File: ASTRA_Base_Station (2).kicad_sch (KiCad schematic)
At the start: 24 parts, among them J2 24V, J3 24V, J4 24V, J5 5V, M1 Stepper_Motor_bipolar, U2 A4988_STEPPER_MOTOR_DRIVER_CA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, U4 D24V22F3, U5 D24V22F5, U6 D24V22F12

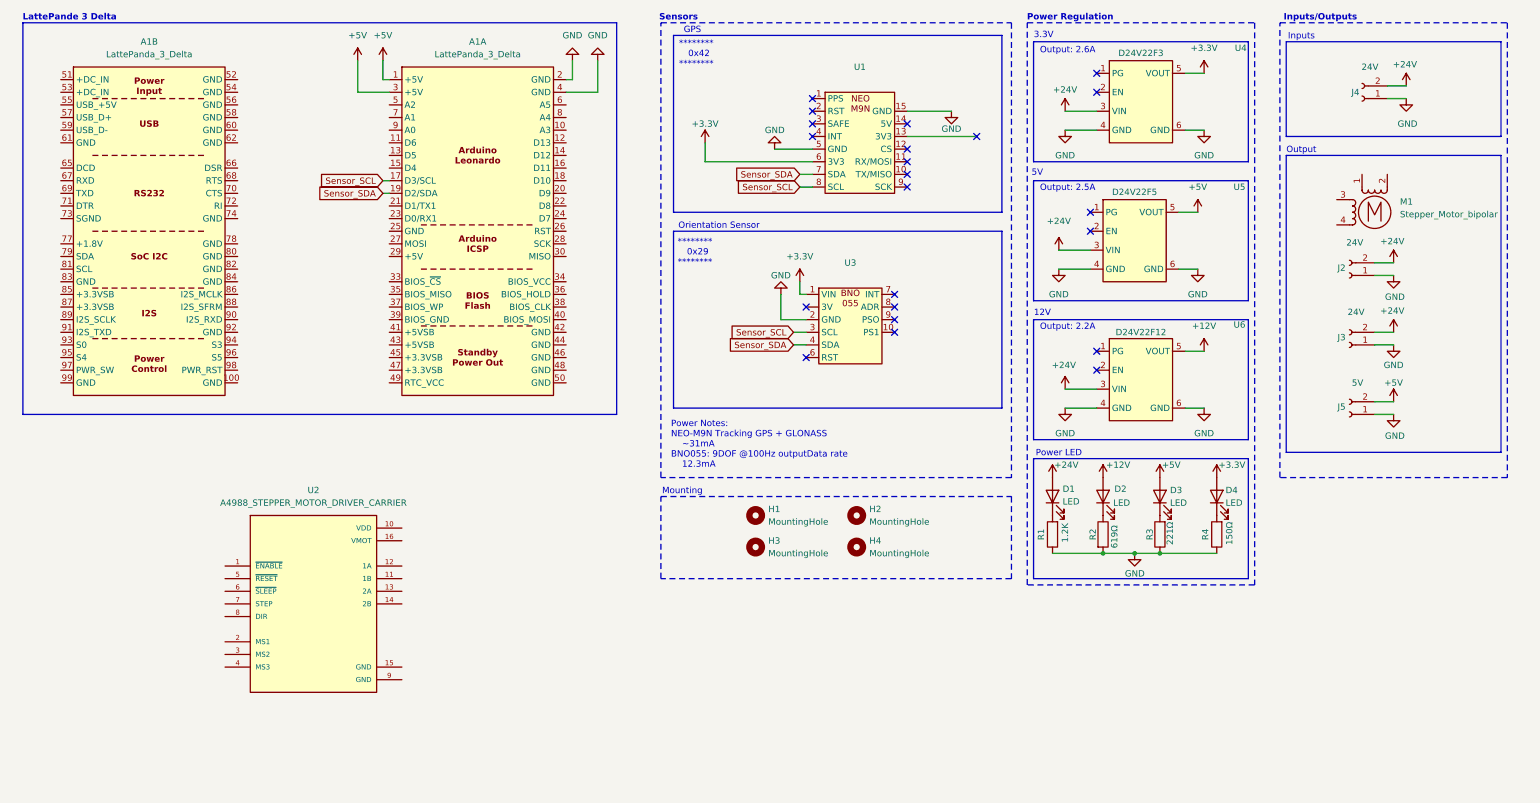
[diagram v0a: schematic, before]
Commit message: Added Motor Driver
Switched the motor driver from the A4988 to the more appropriate DRV8834, added schematic connections to the bipolar stepper motor, updated power regulation, organized schematic sections, and added the LattePanda Delta 3 and DRV8834 footprints to the tracking antenna library
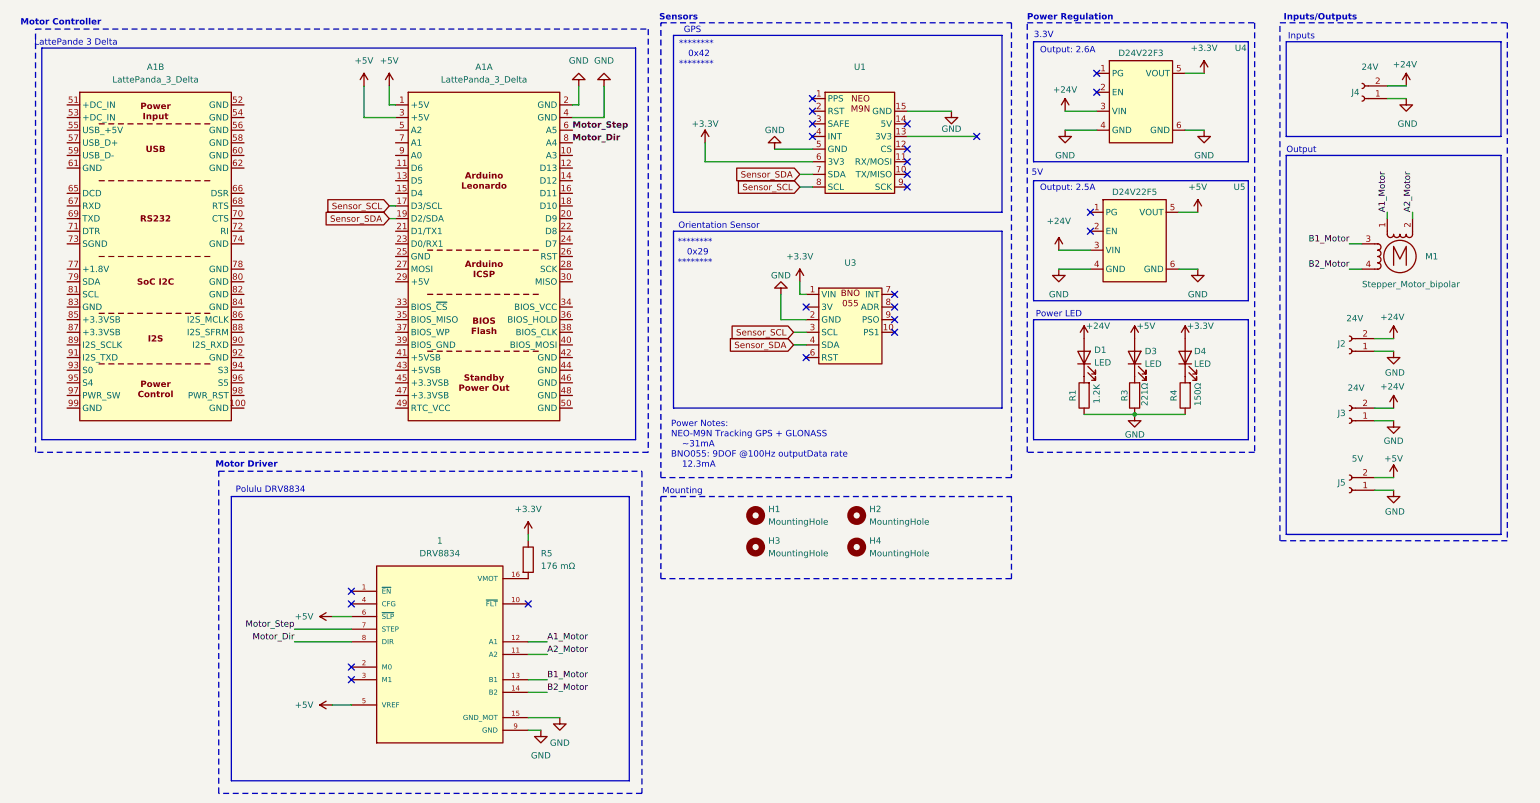
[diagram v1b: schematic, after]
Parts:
- removed D2: LED, Tracking Ant:LED 3mm, symbol Device:LED
- removed R2: 619Ω, Resistor_SMD:R_0603_1608Metric_Pad0.98x0.95mm_HandSolder, symbol Device:R
- removed U2: A4988_STEPPER_MOTOR_DRIVER_CARRIER, symbol Tracking_Antenna_25_Symbols:A4988_STEPPER_MOTOR_DRIVER_CARRIER
- removed U6: D24V22F12, Core_fp:D24V22Fx, symbol Tracking_Antenna_25_Symbols:D24V22Fx
- added 1: DRV8834, symbol Tracking_Antenna_25_Symbols:DRV8834
- added R5: 176 mΩ, symbol Device:R
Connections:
- net +3.3V: now also R5.1
- net +5V: now also 1.5 (VREF), 1.6 (~{SLP})
- net GND: now also 1.15 (GND_MOT), 1.9 (GND)
- net Motor_Step: now reaches A1.6 (A5)
- net Motor_Step: now also 1.7 (STEP)
- net Motor_Dir: now reaches A1.8 (A4)
- net Motor_Dir: now also 1.8 (DIR)
- net A1_Motor: now reaches M1.1
- net A1_Motor: now also 1.12 (A1)
- net A2_Motor: now reaches M1.2 (-)
- net A2_Motor: now also 1.11 (A2)
- net B1_Motor: now reaches M1.3
- net B1_Motor: now also 1.13 (B1)
- net B2_Motor: now reaches M1.4
- net B2_Motor: now also 1.14 (B2)
- new net: 1.16 (VMOT), R5.2
- no-connect marks 22 -> 25
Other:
- note added: "Motor Controller"
- note added: "Motor Driver"
- note added: "Polulu DRV8834"
- note removed: "12V"
- note removed: "Output: 2.2A"
- moved on the sheet: A1A, A1B, D1, D3, D4, J2, J3, J5, M1, R1, R3, R4

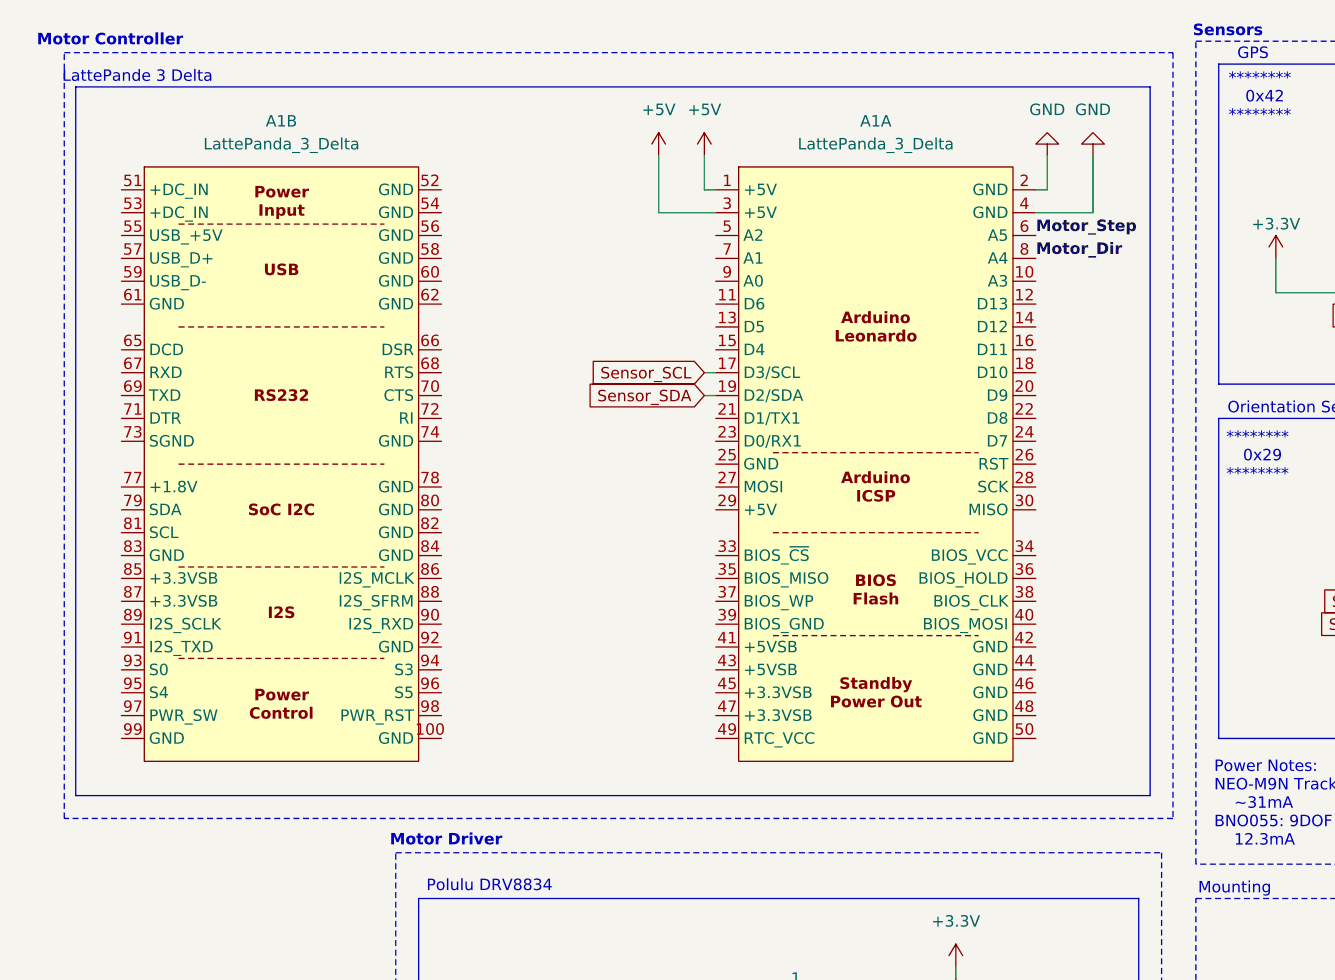
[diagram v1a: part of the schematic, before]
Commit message: PCB Traces Added
Components have been arranged on the PCB and traces added

Motor connector needs to be added, ground plane needs to be added, and organization needed.
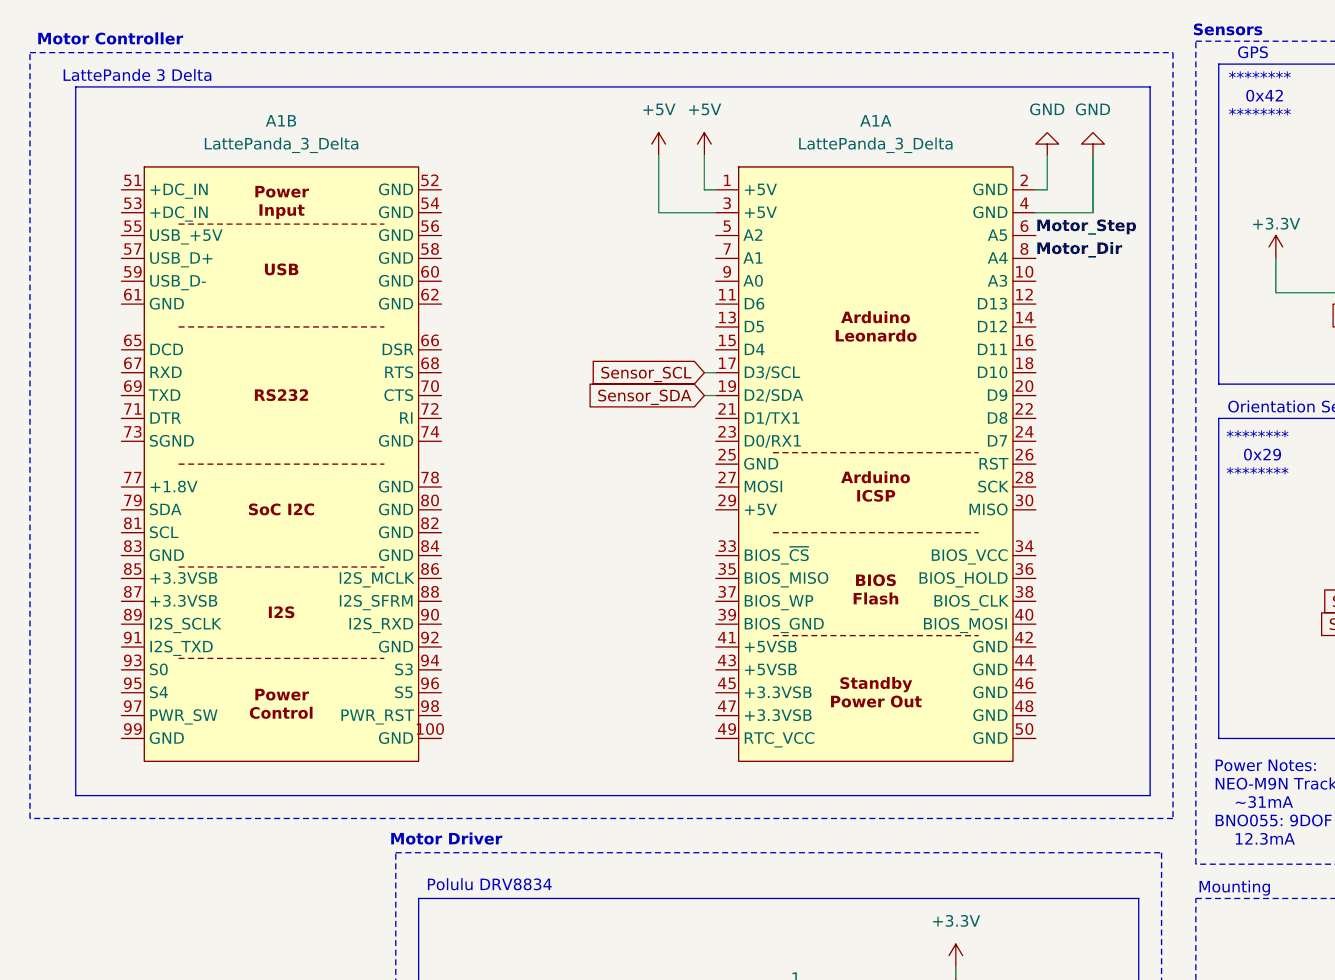
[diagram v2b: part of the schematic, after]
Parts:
- 1: footprint (none) -> Tracking Ant:Polulu_DRV8834
- A1: footprint (none) -> Tracking Ant:LattePanda_3_Delta
- D4: footprint Core_fp:LED 3mm -> Tracking Ant:LED 3mm
- R5: footprint (none) -> Resistor_SMD:R_0603_1608Metric
- U1: footprint TestBed:NEO-M9N -> Tracking Ant:NEO-M9N
- U3: footprint Connector_Molex:Molex_Mini-Fit_Jr_5566-06A_2x03_P4.20mm_Vertical -> Connector_Molex:Molex_Mini-Fit_Jr_5566-04A_2x02_P4.20mm_Vertical
- U4, U5: footprint Core_fp:D24V22Fx -> Tracking Ant:D24V22Fx
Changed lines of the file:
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@@
 	)
 	(rectangle
-		(start 31.75 16.51)
+		(start 27.94 16.51)
 		(end 154.94 101.6)
 		(stroke
@@
 			)
 		)
-		(property "Footprint" "Connector_Molex:Molex_Mini-Fit_Jr_5566-06A_2x03_P4.20mm_Vertical"
+		(property "Footprint" "Connector_Molex:Molex_Mini-Fit_Jr_5566-04A_2x02_P4.20mm_Vertical"
 			(at 195.58 67.31 0)
 			(effects
@@
 			)
 		)
-		(property "Footprint" ""
+		(property "Footprint" "Resistor_SMD:R_0603_1608Metric"
 			(at 129.032 123.19 90)
 			(effects
@@
 			)
 		)
-		(property "Footprint" "TestBed:NEO-M9N"
+		(property "Footprint" "Tracking Ant:NEO-M9N"
 			(at 197.104 24.638 0)
 			(effects
@@
 			)
 		)
-		(property "Footprint" "Core_fp:D24V22Fx"
+		(property "Footprint" "Tracking Ant:D24V22Fx"
 			(at 247.65 22.86 0)
 			(effects
@@
 			)
 		)
-		(property "Footprint" "Core_fp:D24V22Fx"
+		(property "Footprint" "Tracking Ant:D24V22Fx"
 			(at 246.38 50.8 0)
 			(effects
@@
 			)
 		)
-		(property "Footprint" ""
+		(property "Footprint" "Tracking Ant:LattePanda_3_Delta"
 			(at 55.88 62.23 0)
 			(effects
@@
 			)
 		)
-		(property "Footprint" ""
+		(property "Footprint" "Tracking Ant:LattePanda_3_Delta"
 			(at 121.92 62.23 0)
 			(effects
@@
 			)
 		)
-		(property "Footprint" "Core_fp:LED 3mm"
+		(property "Footprint" "Tracking Ant:LED 3mm"
 			(at 262.89 82.55 0)
 			(effects
@@
 			)
 		)
-		(property "Footprint" ""
+		(property "Footprint" "Tracking Ant:Polulu_DRV8834"
 			(at 113.03 142.24 0)
 			(effects

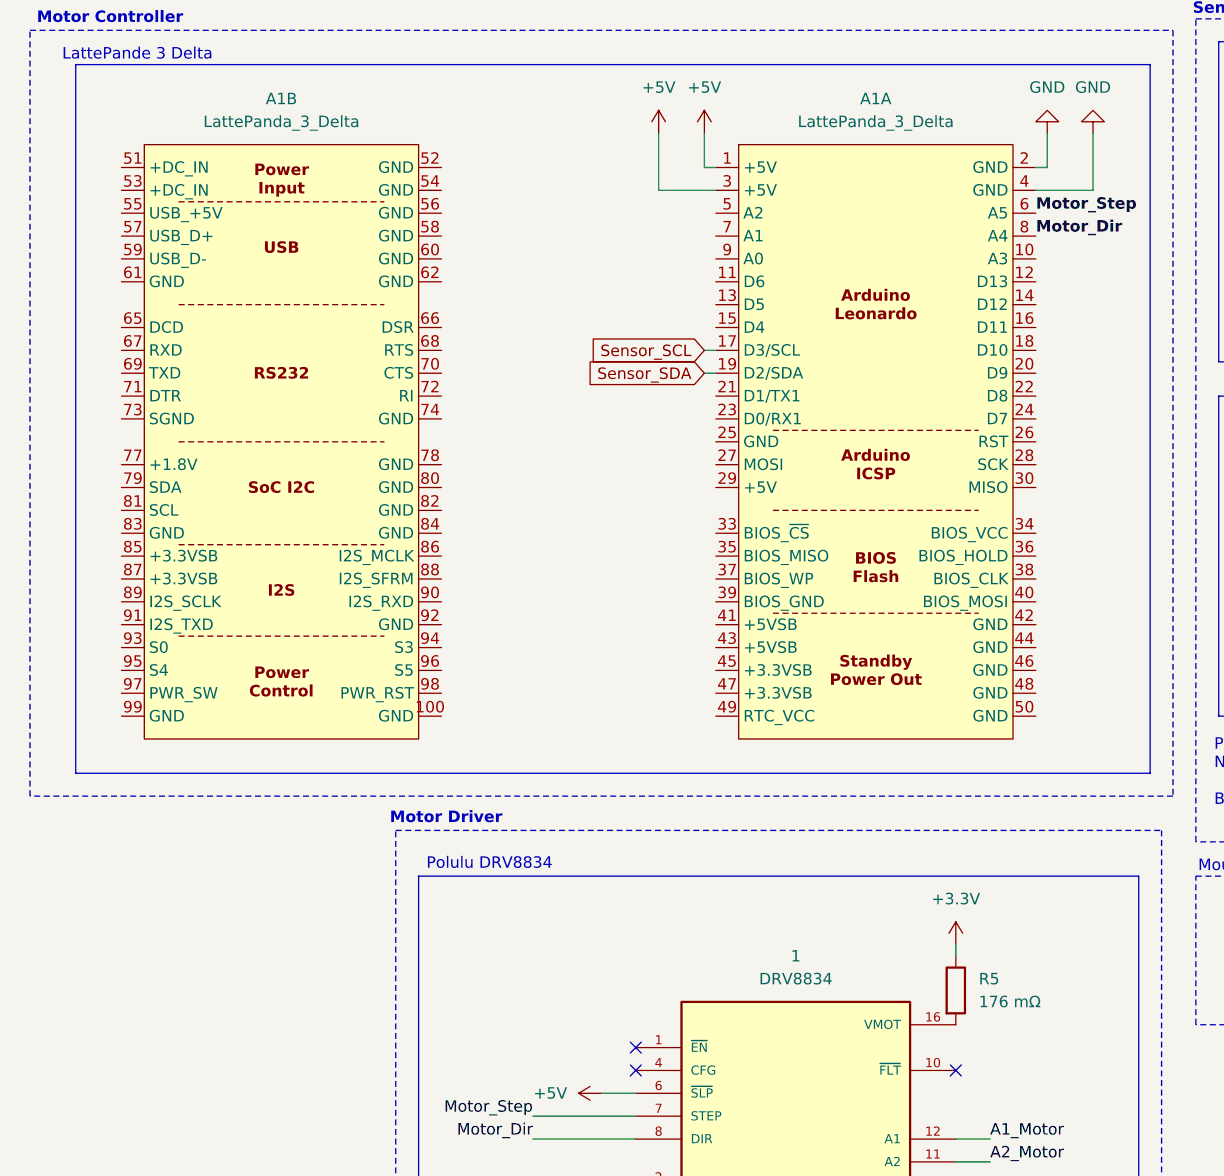
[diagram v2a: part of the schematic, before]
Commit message: PCB Review Draft
All  PCB connections made
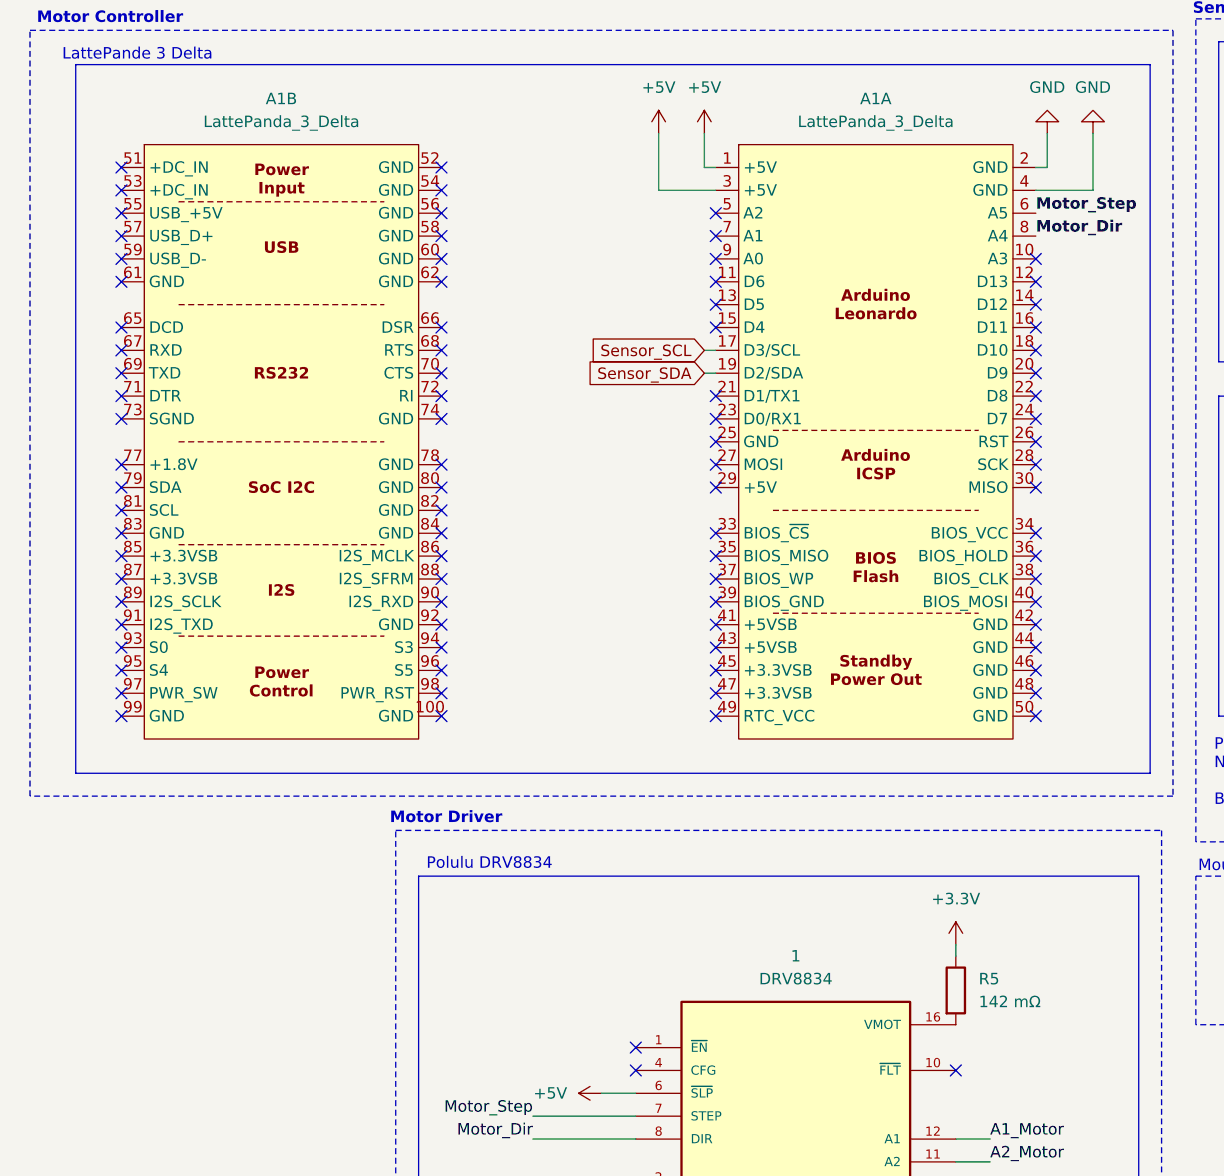
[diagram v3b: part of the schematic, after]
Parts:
- M1: footprint (none) -> Connector_Molex:Molex_Mini-Fit_Jr_5566-04A_2x02_P4.20mm_Vertical
- R5: value 176 mΩ -> 142 mΩ
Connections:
- no-connect marks 25 -> 111

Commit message: Tracking Antenna PCB V2 Finished
Tracking Antenna PCB V2 Finished, files renamed for easier understanding
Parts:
- removed R5: 142 mΩ, Resistor_SMD:R_0603_1608Metric, symbol Device:R
- removed U3: ~, Connector_Molex:Molex_Mini-Fit_Jr_5566-04A_2x02_P4.20mm_Vertical, symbol Tracking_Antenna_25_Symbols:BNO-055
- added C1: 0.1 uF, Capacitor_SMD:C_0603_1608Metric_Pad1.08x0.95mm_HandSolder, symbol Device:C
- added D2: Inolux_IN-PI554FCH, LED_SMD:LED_Inolux_IN-PI554FCH_PLCC4_5.0x5.0mm_P3.2mm, symbol LED:Inolux_IN-PI554FCH
- added J6: Conn_01x04_Socket, Connector_Molex:Molex_Mini-Fit_Jr_5566-04A_2x02_P4.20mm_Vertical, symbol Connector:Conn_01x04_Socket
- M1: value Stepper_Motor_bipolar -> Stepper Motor
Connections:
- net +3.3V: now also 1.16 (VMOT), 1.6 (~{SLP}), J6.2 (Pin_2)
- net +5V: now also C1.1, D2.3 (VDD); no longer 1.6 (~{SLP})
- net A2_Motor: now also M1.3; no longer M1.2 (-)
- net B1_Motor: now also M1.2 (-); no longer M1.3
- net GND: now also C1.2, D2.1 (VSS), J6.1 (Pin_1)
- net Motor_Dir: now also A1.12 (D13); no longer A1.8 (A4)
- net Motor_Step: now also A1.10 (A3); no longer A1.6 (A5)
- net Sensor_SCL: now also J6.4 (Pin_4)
- net Sensor_SDA: now also J6.3 (Pin_3)
- net NEO_LED_DIN: now reaches A1.24 (D7)
- net NEO_LED_DIN: now also D2.2 (DIN)
- net EN_Driver: now reaches 1.1 (~{EN})
- net EN_Driver: now also A1.8 (A4)
- no-connect marks 111 -> 101
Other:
- note added: "BNO055"
- note added: "Ethernet Switch"
- note added: "Neo LED"
- note added: "POE Injectors"
- note added: "Polulu DRV8834 (Pololu item #: 2134)"
- note added: "Using a low-voltage motor driver because the stepper motor takes 3.06 V"
- note removed: "Polulu DRV8834"
- moved on the sheet: J5
